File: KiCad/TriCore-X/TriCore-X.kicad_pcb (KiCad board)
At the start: 6 copper layers, 100 x 100 mm, 52 parts, among them J1 PJ-035DH, J2 877159106, J3 LPJG0926HENL, J4 1054500101, J5 USB-A-D-X-X-TH-R, Q1 AOD407, U1 RK3568B2, U2 XC7A100T-FGG484, U3 TPS56637RPAR, U4 TPS56637RPAR, U5 RK809-5, U6 ESP32-S3-WROOM-1

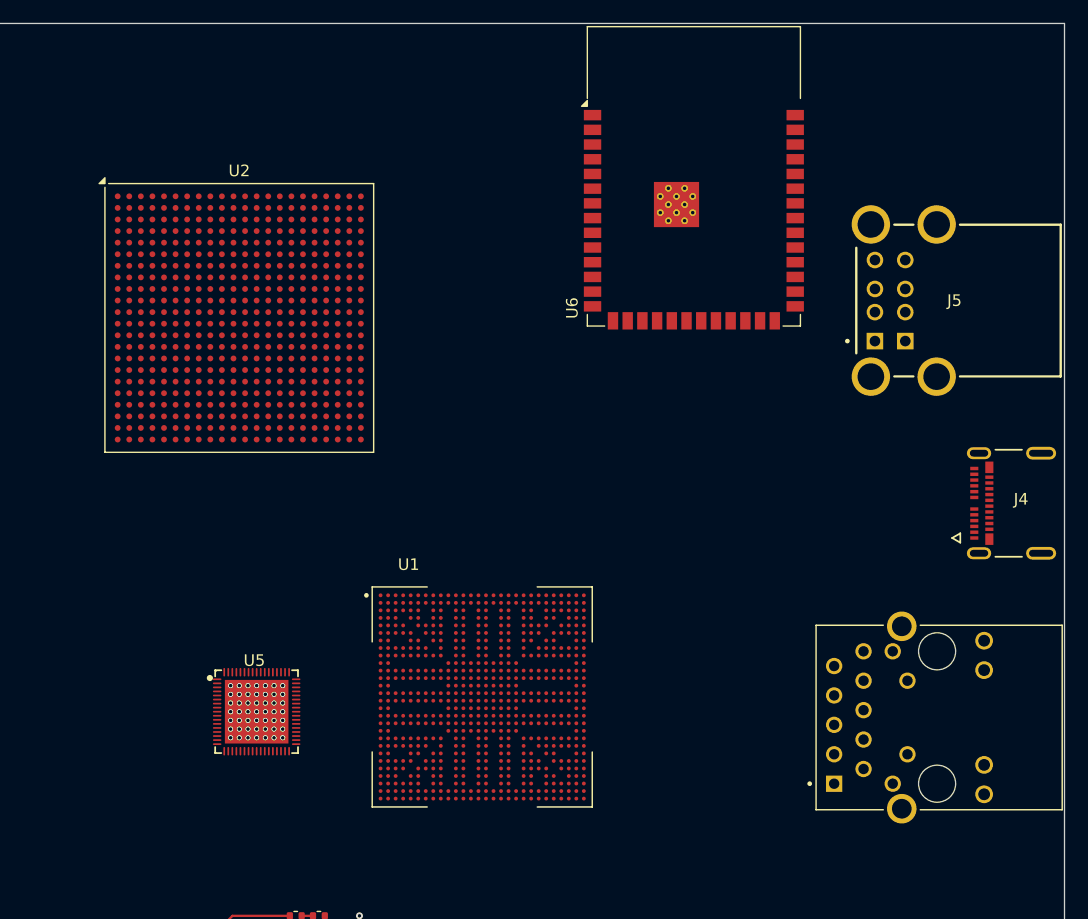
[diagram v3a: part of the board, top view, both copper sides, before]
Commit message: refactor: change core MCU to STM32H723 and add LPDDR4/HDMI support
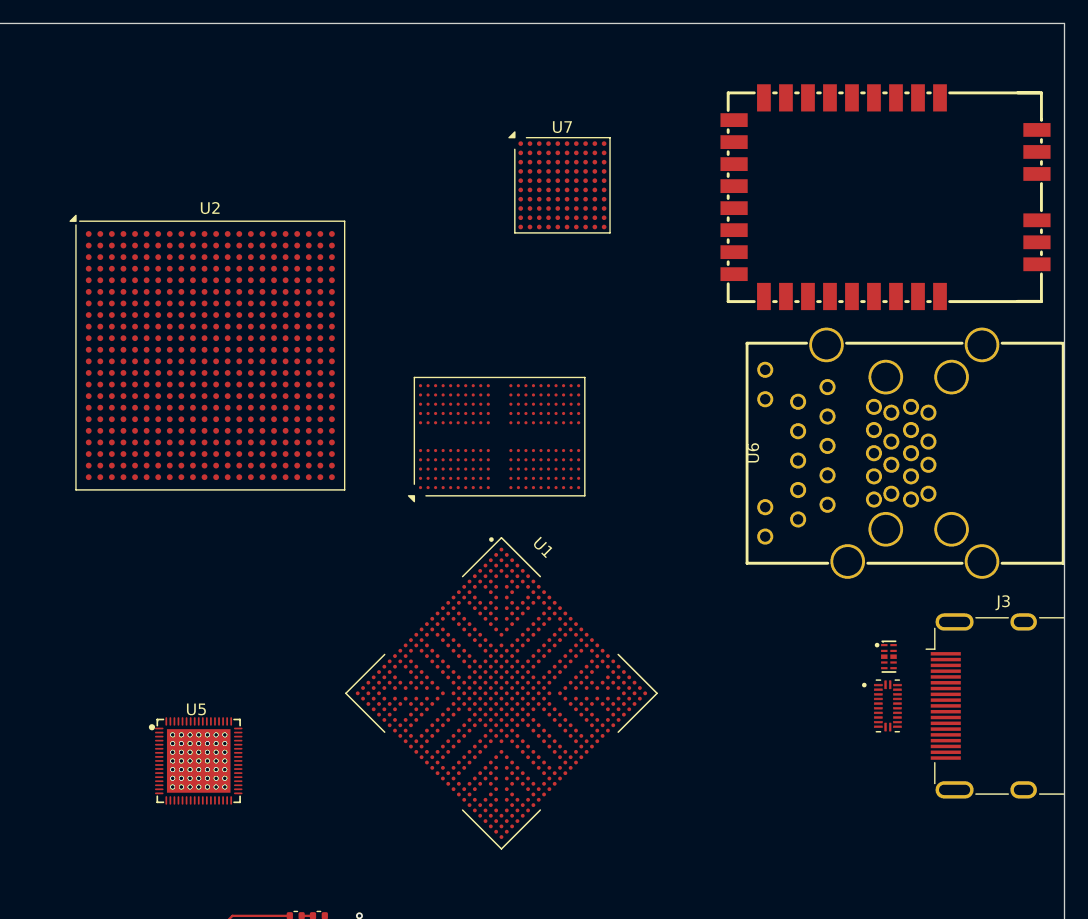
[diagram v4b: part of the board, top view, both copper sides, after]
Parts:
- removed J4: 1054500101, TYPE-C:MOLEX_1054500101
- removed J5: USB-A-D-X-X-TH-R, TYPE-A:SAMTEC_USB-A-D-X-X-TH-R
- added D3: ESD224DQAR, ESD224DQAR:USON-10_L2.5-W1.0-P0.50-BL, F.Cu at (178.4, 100.5)
- added U7: STM32H723VGHx, Package_BGA:TFBGA-100_8x8mm_Layout10x10_P0.8mm, F.Cu at (150.4, 59.8)
- added U8: IS43LQ32256AL-062BLI, Package_BGA:BGA-200_10x14.5mm_Layout12x22_P0.8x0.65mm, F.Cu at (145.0, 81.5)
- added U9: TPD12S016RKTR, TPD12S016RKTR:IC_TPD12S016RKTR, F.Cu at (178.5, 104.8)
- added WIFI1: BL-M8822CU3-A, BL-M8822CU3-A:WIRELM-SMD_BL-M8822CU3-A, F.Cu at (178.3, 60.8)
- J3: value LPJG0926HENL -> HDMI_A; footprint LPJG0926HENL:LINK-PP_LPJG0926HENL -> Connector_Video:HDMI_A_Molex_208658-1001_Horizontal
- U6: value ESP32-S3-WROOM-1 -> JFM38U1B-B313-4F; footprint RF_Module:ESP32-S3-WROOM-1 -> JFM38U1B-B313-4F:RJ45-TH_JFM38U11-B31X-4F
- moved U6 30.1 mm to (180.0, 82.9), turned to 90 degrees
- moved U5 6.56 mm to (118.8, 109.5)
- moved J3 4.16 mm to (186.8, 104.8), turned to 0 degrees
- moved U2 4.10 mm to (120.0, 74.5)
- moved U1 1.69 mm to (145.1, 103.7), turned to -45 degrees
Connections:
- J3 pad 4: Net-(J3-CT-Pad4) -> unconnected-(J3-D1+-Pad4)
- J3 pad 5: Net-(J3-CT-Pad4) -> unconnected-(J3-D1S-Pad5)
- U1 pad A11: unconnected-(U1E-DDR_DQS0P_B-PadA11) -> /DDR4/DDR_DQS0P_B
- U1 pad A15: unconnected-(U1E-DDR_DQS1N_B-PadA15) -> /DDR4/DDR_DQS1P_B
- U1 pad A2: unconnected-(U1E-AC25-PadA2) -> /DDR4/DDR_CS0N_A
- U1 pad A4: unconnected-(U1E-AC24-PadA4) -> /DDR4/DDR_CLKN_A
- U1 pad A5: unconnected-(U1E-AC9-PadA5) -> /DDR4/DDR_CLKN_B
- U1 pad A7: unconnected-(U1E-AC6-PadA7) -> /DDR4/DDR_CA1_B
- U1 pad A8: unconnected-(U1E-AC7-PadA8) -> /DDR4/DDR_ODT_CA_B
- U1 pad B1: unconnected-(U1E-AC2-PadB1) -> /DDR4/DDR_CA1_A
- U1 pad B11: unconnected-(U1E-DDR_DQS0N_B-PadB11) -> /DDR4/DDR_DQS0N_B
- U1 pad B15: unconnected-(U1E-DDR_DQS1P_B-PadB15) -> /DDR4/DDR_DQS1N_B
- U1 pad B3: unconnected-(U1E-AC22-PadB3) -> /DDR4/DDR_CKE0_A
- U1 pad B4: unconnected-(U1E-AC23-PadB4) -> /DDR4/DDR_CLKP_A
- U1 pad B6: unconnected-(U1E-AC0-PadB6) -> /DDR4/DDR_CLKP_B
- U1 pad B7: unconnected-(U1E-AC5-PadB7) -> /DDR4/DDR_CA5_B
- U1 pad B8: unconnected-(U1E-AC13-PadB8) -> /DDR4/DDR_CA0_B
- U1 pad C1: unconnected-(U1E-AC8-PadC1) -> /DDR4/DDR_ODT_CA_A
- U1 pad C2: unconnected-(U1E-AC11-PadC2) -> /DDR4/DDR_CA0_A
- U1 pad C4: unconnected-(U1E-AC12-PadC4) -> /DDR4/DDR_CA3_A
- U1 pad C5: unconnected-(U1E-AC14-PadC5) -> /DDR4/DDR_CA4_A
- U1 pad D14: unconnected-(U1E-DDR_DM0_B-PadD14) -> /DDR4/DDR_DM0_B
- U1 pad D5: unconnected-(U1E-AC16-PadD5) -> /DDR4/DDR_CA5_A
- U1 pad D6: unconnected-(U1E-AC10-PadD6) -> /DDR4/DDR_CKE0_B
- U1 pad D8: unconnected-(U1E-AC28-PadD8) -> /DDR4/DDR_CS0N_B
- U1 pad D9: unconnected-(U1E-AC4-PadD9) -> /DDR4/DDR_CA3_B
- U1 pad E11: unconnected-(U1E-AC18-PadE11) -> /DDR4/DDR_CA2_B
- U1 pad E17: unconnected-(U1E-DDR_DM1_B-PadE17) -> /DDR4/DDR_DM1_B
- U1 pad E4: unconnected-(U1E-AC15-PadE4) -> /DDR4/DDR_CA2_A
- U1 pad E9: unconnected-(U1E-AC19-PadE9) -> /DDR4/DDR_CA4_B
- U1 pad F11: unconnected-(U1E-AC29-PadF11) -> /DDR4/DDR_RESETN
- U1 pad G1: unconnected-(U1E-DDR_DQS0P_A-PadG1) -> /DDR4/DDR_DQS0P_A
- U1 pad G2: unconnected-(U1E-DDR_DQS0N_A-PadG2) -> /DDR4/DDR_DQS0N_A
- U1 pad H5: unconnected-(U1E-DDR_DM0_A-PadH5) -> /DDR4/DDR_DM0_A
- U1 pad J4: unconnected-(U1E-DDR_DM1_A-PadJ4) -> /DDR4/DDR_DM1_A
- U1 pad L1: unconnected-(U1E-DDR_DQS1N_A-PadL1) -> /DDR4/DDR_DQS1N_A
- U1 pad L2: unconnected-(U1E-DDR_DQS1P_A-PadL2) -> /DDR4/DDR_DQS1P_A
- U6 pad 1: GND -> unconnected-(U6-VBUS-Pad1)
- U6 pad 13: unconnected-(U6-USB_D--Pad13) -> GND
- U6 pad 16: unconnected-(U6-IO46-Pad16) -> GND
- U6 pad 17: RK3568_SDIO_D2 -> unconnected-(U6-SRDA_SSTX--Pad17)
- U6 pad 18: RK3568_SDIO_D3 -> unconnected-(U6-STDA_SSTX+-Pad18)
- U6 pad 19: RK3568_SDIO_CMD -> unconnected-(U6-VCT-Pad19)
- U6 pad 20: RK3568_SDIO_CLK -> unconnected-(U6-D1+-Pad20)
- U6 pad 21: RK3568_SDIO_D0 -> unconnected-(U6-D1--Pad21)
- U6 pad 22: RK3568_SDIO_D1 -> unconnected-(U6-D2+-Pad22)
- U6 pad 28: unconnected-(U6-IO35-Pad28) -> GND
- U6 pad 3: ESP32_EN -> unconnected-(U6-D+-Pad3)
- U6 pad 4: unconnected-(U6-IO4-Pad4) -> GND
- U6 pad 40: GND -> unconnected-(U6-SHELL-Pad40)
- U6 pad 7: unconnected-(U6-IO7-Pad7) -> GND

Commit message: feat: complete schematic for RK809-5 PMIC peripheral circuits
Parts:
- added C19: 18pF, Capacitor_SMD:C_0402_1005Metric, F.Cu at (149.5, 121.5)
- added C20: 18pF, Capacitor_SMD:C_0402_1005Metric, F.Cu at (149.5, 123.5)
- added C21: 1uF, Capacitor_SMD:C_0402_1005Metric, F.Cu at (57.2, 106.0)
- added C22: 1uF, Capacitor_SMD:C_0402_1005Metric, F.Cu at (57.2, 108.0)
- added C23: 1uF, Capacitor_SMD:C_0402_1005Metric, F.Cu at (57.2, 109.9)
- added C24: 1uF, Capacitor_SMD:C_0402_1005Metric, F.Cu at (57.2, 111.9)
- added C25: 1uF, Capacitor_SMD:C_0402_1005Metric, F.Cu at (57.2, 113.9)
- added C26: 1uF, Capacitor_SMD:C_0402_1005Metric, F.Cu at (57.2, 115.8)
- added C27: 1uF, Capacitor_SMD:C_0402_1005Metric, F.Cu at (57.2, 117.8)
- added C28: 1uF, Capacitor_SMD:C_0402_1005Metric, F.Cu at (60.0, 106.0)
- added C29: 1uF, Capacitor_SMD:C_0402_1005Metric, F.Cu at (60.0, 108.0)
- added C30: 1uF, Capacitor_SMD:C_0402_1005Metric, F.Cu at (60.0, 109.9)
- added C31: 1uF, Capacitor_SMD:C_0402_1005Metric, F.Cu at (60.0, 111.9)
- added C32: 1uF, Capacitor_SMD:C_0402_1005Metric, F.Cu at (60.0, 113.9)
- added C33: 1uF, Capacitor_SMD:C_0402_1005Metric, F.Cu at (60.0, 115.8)
- added C34: 1uF, Capacitor_SMD:C_0402_1005Metric, F.Cu at (60.0, 117.8)
- added C35: 1uF, Capacitor_SMD:C_0402_1005Metric, F.Cu at (62.9, 106.0)
- added C36: 1uF, Capacitor_SMD:C_0402_1005Metric, F.Cu at (62.9, 108.0)
- added C37: 1uF, Capacitor_SMD:C_0402_1005Metric, F.Cu at (62.9, 109.9)
- added C38: 2.2uF, Capacitor_SMD:C_0402_1005Metric, F.Cu at (62.9, 111.9)
- added C39: 2.2uF, Capacitor_SMD:C_0402_1005Metric, F.Cu at (62.9, 113.9)
- added C40: 1uF, Capacitor_SMD:C_0402_1005Metric, F.Cu at (62.9, 115.8)
- added C41: 1uF, Capacitor_SMD:C_0402_1005Metric, F.Cu at (62.9, 117.8)
- added C42: 1uF, Capacitor_SMD:C_0402_1005Metric, F.Cu at (65.8, 106.0)
- added C43: 1uF, Capacitor_SMD:C_0402_1005Metric, F.Cu at (65.8, 108.0)
- added C44: 10uF, Capacitor_SMD:C_0402_1005Metric, F.Cu at (65.8, 109.9)
- added C45: 1uF, Capacitor_SMD:C_0402_1005Metric, F.Cu at (65.8, 111.9)
- added C46: 10uF, Capacitor_SMD:C_0402_1005Metric, F.Cu at (65.8, 113.9)
- added C47: 10uF, Capacitor_SMD:C_0402_1005Metric, F.Cu at (65.8, 115.8)
- added C48: 10uF, Capacitor_SMD:C_0402_1005Metric, F.Cu at (65.8, 117.8)
- added C49: 10uF, Capacitor_SMD:C_0402_1005Metric, F.Cu at (68.5, 106.0)
- added C50: 10uF, Capacitor_SMD:C_0402_1005Metric, F.Cu at (68.6, 108.0)
- added C51: 22uF, Capacitor_SMD:C_0805_2012Metric, F.Cu at (58.0, 91.5)
- added C52: 22uF, Capacitor_SMD:C_0805_2012Metric, F.Cu at (58.0, 94.5)
- added C53: 22uF, Capacitor_SMD:C_0805_2012Metric, F.Cu at (58.0, 97.5)
- added C54: 22uF, Capacitor_SMD:C_0805_2012Metric, F.Cu at (58.0, 100.5)
- added C55: 22uF, Capacitor_SMD:C_0805_2012Metric, F.Cu at (58.0, 103.5)
- added C56: 22uF, Capacitor_SMD:C_0805_2012Metric, F.Cu at (62.4, 91.5)
- added C57: 22uF, Capacitor_SMD:C_0805_2012Metric, F.Cu at (62.4, 94.5)
- added C58: 22uF, Capacitor_SMD:C_0805_2012Metric, F.Cu at (62.4, 97.5)
- added C59: 22uF, Capacitor_SMD:C_0805_2012Metric, F.Cu at (62.4, 100.5)
- added C60: 22uF, Capacitor_SMD:C_0805_2012Metric, F.Cu at (62.4, 103.5)
- added C61: 100nF, Capacitor_SMD:C_0402_1005Metric, F.Cu at (68.6, 109.9)
- added C62: 100nF, Capacitor_SMD:C_0402_1005Metric, F.Cu at (68.6, 111.9)
- added C63: 100nF, Capacitor_SMD:C_0402_1005Metric, F.Cu at (68.6, 113.9)
- added L3: FNR6045SR47NT, L_6045:IND-SMD_L6.0-W6.0_FNR60XXS, F.Cu at (51.6, 93.6)
- added L4: FNR6045SR47NT, L_6045:IND-SMD_L6.0-W6.0_FNR60XXS, F.Cu at (51.6, 100.8)
- added L5: FNR6045SR47NT, L_6045:IND-SMD_L6.0-W6.0_FNR60XXS, F.Cu at (51.6, 108.1)
- added L6: FNR6045SR47NT, L_6045:IND-SMD_L6.0-W6.0_FNR60XXS, F.Cu at (51.6, 115.3)
- added L7: FNR6045SR47NT, L_6045:IND-SMD_L6.0-W6.0_FNR60XXS, F.Cu at (51.6, 122.6)
- added R16: 1M, Resistor_SMD:R_0402_1005Metric, F.Cu at (154.7, 117.0)
- added R17: 22R, Resistor_SMD:R_0402_1005Metric, F.Cu at (154.7, 119.0)
- added R18: 82K, Resistor_SMD:R_0402_1005Metric, F.Cu at (57.2, 119.8)
- added R19: 120K, Resistor_SMD:R_0402_1005Metric, F.Cu at (57.2, 121.8)
- added R20: 4.7K, Resistor_SMD:R_0402_1005Metric, F.Cu at (57.2, 123.8)
- added R21: 4.7K, Resistor_SMD:R_0402_1005Metric, F.Cu at (60.1, 119.8)
- added R22: 100K, Resistor_SMD:R_0402_1005Metric, F.Cu at (60.1, 121.8)
- added R23: 22K, Resistor_SMD:R_0402_1005Metric, F.Cu at (60.1, 123.8)
- added R24: 10K, Resistor_SMD:R_0402_1005Metric, F.Cu at (63.0, 119.8)
- added R25: 10K, Resistor_SMD:R_0402_1005Metric, F.Cu at (63.0, 121.8)
- added R26: 10K, Resistor_SMD:R_0402_1005Metric, F.Cu at (63.0, 123.8)
- added U10: USB3300-EZK-TR, USB3300-EZK-TR:QFN50P500X500X100-33N, F.Cu at (153.8, 67.0)
- added Y1: 32.768KHZ, Crystal:Crystal_DS26_D2.0mm_L6.0mm_Vertical, F.Cu at (65.7, 120.8)
- added Y2: Crystal_GND24, Crystal:Crystal_SMD_3225-4Pin_3.2x2.5mm, F.Cu at (150.7, 117.4)
- moved U7 10.2 mm to (142.1, 65.7)
- moved U5 6.08 mm to (117.8, 103.5)
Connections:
- net /DDR4/DDR_CLKN_A renamed /DDR4/DDR_CLK_A_N
- net /DDR4/DDR_CLKN_B renamed /DDR4/DDR_CLK_B_N
- net /DDR4/DDR_CLKP_A renamed /DDR4/DDR_CLK_A_P
- net /DDR4/DDR_CLKP_B renamed /DDR4/DDR_CLK_B_P
- net /DDR4/DDR_DQS0N_A renamed /DDR4/DDR_DQS0_A_N
- net /DDR4/DDR_DQS0N_B renamed /DDR4/DDR_DQS0_B_N
- net /DDR4/DDR_DQS0P_A renamed /DDR4/DDR_DQS0_A_P
- net /DDR4/DDR_DQS0P_B renamed /DDR4/DDR_DQS0_B_P
- net /DDR4/DDR_DQS1N_A renamed /DDR4/DDR_DQS1_A_N
- net /DDR4/DDR_DQS1N_B renamed /DDR4/DDR_DQS1_B_N
- net /DDR4/DDR_DQS1P_A renamed /DDR4/DDR_DQS1_A_P
- net /DDR4/DDR_DQS1P_B renamed /DDR4/DDR_DQS1_B_P
- U1 pad AF27: unconnected-(U1F-XOUT24M-PadAF27) -> Net-(U1F-XOUT24M)
- U1 pad AF28: unconnected-(U1F-XIN24M-PadAF28) -> Net-(U1F-XIN24M)
- U5 pad 1: unconnected-(U5-SCL-Pad1) -> /power/RK809-5_SDA
- U5 pad 10: unconnected-(U5-VCC2-Pad10) -> +5V
- U5 pad 11: unconnected-(U5-VCC1-Pad11) -> +5V
- U5 pad 12: unconnected-(U5-SW1-Pad12) -> Net-(U5-SW1)
- U5 pad 13: unconnected-(U5-FB1-Pad13) -> /power/BUCK1
- U5 pad 14: unconnected-(U5-LRCLK-Pad14) -> GND
- U5 pad 15: unconnected-(U5-BCLK-Pad15) -> GND
- U5 pad 16: unconnected-(U5-MCLK-Pad16) -> GND
- U5 pad 17: unconnected-(U5-SDI-Pad17) -> GND
- U5 pad 19: unconnected-(U5-PDMCLK-Pad19) -> GND
- U5 pad 2: unconnected-(U5-SDA-Pad2) -> /power/RK809-5_SCL
- U5 pad 20: unconnected-(U5-LDO3-Pad20) -> /power/VLDO3
- U5 pad 21: unconnected-(U5-LDO2-Pad21) -> /power/VLDO2
- U5 pad 22: unconnected-(U5-VCC5-Pad22) -> /power/VCC SYS
- U5 pad 23: unconnected-(U5-LDO1-Pad23) -> /power/VLDOI
- U5 pad 24: unconnected-(U5-VCC3-Pad24) -> +5V
- U5 pad 25: unconnected-(U5-SW3-Pad25) -> Net-(U5-SW3)
- U5 pad 26: unconnected-(U5-VBUCK3-Pad26) -> /power/BUCK3
- U5 pad 27: unconnected-(U5-FB3-Pad27) -> Net-(U5-FB3)
- U5 pad 28: unconnected-(U5-LDO4-Pad28) -> /power/VLDO4
- U5 pad 29: unconnected-(U5-LDO5-Pad29) -> /power/VLDO5
- U5 pad 3: unconnected-(U5-LDO7-Pad3) -> /power/VLDO7
- U5 pad 30: unconnected-(U5-VCC6-Pad30) -> /power/BUCK 5
- U5 pad 31: unconnected-(U5-LDO6-Pad31) -> /power/VLDO6
- U5 pad 33: unconnected-(U5-VCC_SPK_HP-Pad33) -> +5V
- U5 pad 35: unconnected-(U5-VCC_CPVSS-Pad35) -> Net-(U5-VCC_CPVSS)
- U5 pad 36: unconnected-(U5-CPN-Pad36) -> Net-(U5-CPN)
- U5 pad 37: unconnected-(U5-CPP-Pad37) -> Net-(U5-CPP)
- U5 pad 38: unconnected-(U5-VCC_CPVDD-Pad38) -> Net-(U5-VCC_CPVDD)
- U5 pad 4: unconnected-(U5-VCC7-Pad4) -> /power/BUCK5
- U5 pad 40: unconnected-(U5-HP_SNS-Pad40) -> GND
- U5 pad 44: unconnected-(U5-VCC_1P8A-Pad44) -> Net-(U5-VCC_1P8A)
- U5 pad 45: unconnected-(U5-VCC_RTC-Pad45) -> /power/VCC_RTC
- U5 pad 46: unconnected-(U5-VREF-Pad46) -> Net-(U5-VREF)
- U5 pad 47: unconnected-(U5-GNDREF-Pad47) -> GND
- U5 pad 48: unconnected-(U5-VCC_1P8D-Pad48) -> Net-(U5-VCC_1P8D)
- U5 pad 5: unconnected-(U5-LDO8-Pad5) -> /power/VLDO8
- U5 pad 50: unconnected-(U5-XIN-Pad50) -> Net-(U5-XIN)
- U5 pad 51: unconnected-(U5-XOUT-Pad51) -> Net-(U5-XOUT)
- U5 pad 53: unconnected-(U5-SW5-Pad53) -> Net-(U5-SW5)
- U5 pad 54: unconnected-(U5-VCC9-Pad54) -> +5V
- U5 pad 55: unconnected-(U5-SWOUT1-Pad55) -> /power/VSWOUTI
- U5 pad 56: unconnected-(U5-BATDIV-Pad56) -> GND
- U5 pad 57: unconnected-(U5-VCC8-Pad57) -> /power/BUCK5
- U5 pad 58: unconnected-(U5-SWOUT2-Pad58) -> /power/VSWOUT2
- U5 pad 59: unconnected-(U5-FB5-Pad59) -> /power/BUCK5
- U5 pad 6: unconnected-(U5-LDO9-Pad6) -> /power/VLDO9
- U5 pad 61: unconnected-(U5-VDC-Pad61) -> Net-(U5-VDC)
- U5 pad 62: unconnected-(U5-SNSP-Pad62) -> GND
- U5 pad 63: unconnected-(U5-SNSN-Pad63) -> GND
- U5 pad 64: unconnected-(U5-FB4-Pad64) -> /power/BUCK4
- U5 pad 65: unconnected-(U5-SW4-Pad65) -> Net-(U5-SW4)
- U5 pad 66: unconnected-(U5-VCC4-Pad66) -> +5V
- U5 pad 67: unconnected-(U5-RESETB-Pad67) -> Net-(U5-RESETB)
- U5 pad 68: unconnected-(U5-CLK32K-Pad68) -> Net-(U5-CLK32K)
- U5 pad 7: unconnected-(U5-INT-Pad7) -> Net-(U5-INT)
- U5 pad 8: unconnected-(U5-FB2-Pad8) -> /power/BUCK2
- U5 pad 9: unconnected-(U5-SW2-Pad9) -> Net-(U5-SW2)
